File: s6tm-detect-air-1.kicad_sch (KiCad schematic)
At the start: 72 parts, among them J1 Conn_01x04, J2 TC2030, J3 Conn_01x04, J4 Conn_01x04, J5 Conn_01x04_Pin, SW1 SW_Push, SW2 SW_Push, U1 SYS1002-H2, U10 004-1-0100, U2 MiCS-5524, U3 LMC6482, U4 HT753-1, U5 SN65HVD230, U6 STM32F103C8Tx, U7 HTU21, U8 LM73100, U9 ENS16x, Y1 8M

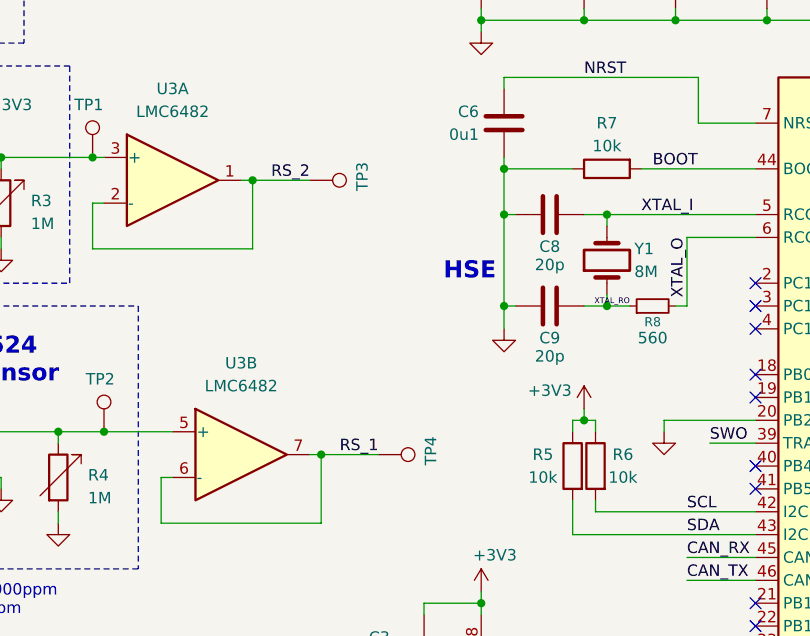
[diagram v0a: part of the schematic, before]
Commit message: pcb: import 2 layer jlc stackup
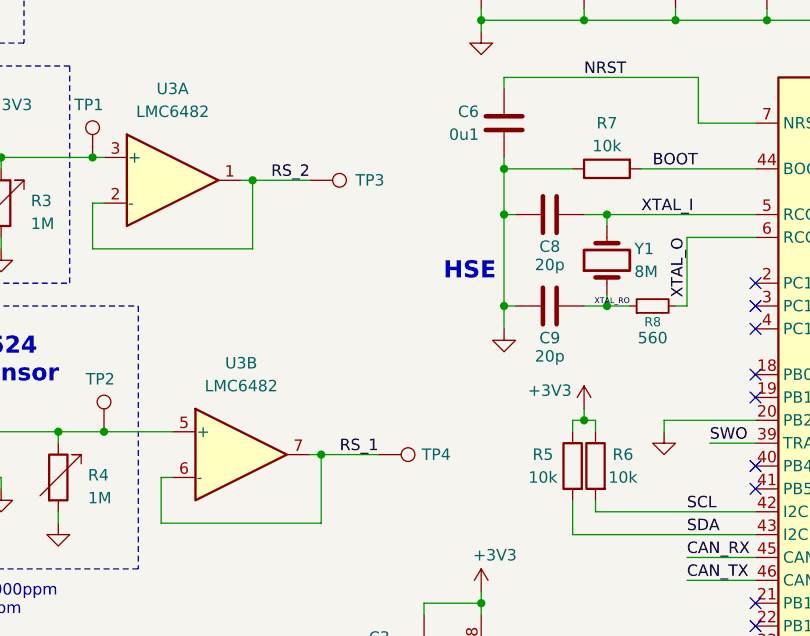
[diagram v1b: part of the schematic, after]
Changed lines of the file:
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@@
 		(dnp no)
 		(property "Reference" "TP4"
-			(at 94.742 99.568 0)
+			(at 93.726 101.6 90)
 			(show_name no)
 			(do_not_autoplace no)
@@
 		(dnp no)
 		(property "Reference" "TP3"
-			(at 87.122 69.088 0)
-			(show_name no)
-			(do_not_autoplace no)
+			(at 86.36 71.12 90)
+			(show_name no)
+			(do_not_autoplace no)

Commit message: pcb: add pwr layout
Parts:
- removed D6: H5VU10U, GLCS:Diode_DFN1006, symbol GLCS:H5VU10U
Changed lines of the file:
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@@
 	)
 	(junction
-		(at 162.56 184.15)
-		(diameter 0)
-		(color 0 0 0 0)
-	)
-	(junction
 		(at 151.13 55.88)
 		(diameter 0)
@@
 	(wire
 		(pts
-			(xy 162.56 184.15) (xy 158.75 184.15)
-		)
-		(stroke
-			(width 0)
-			(type default)
-		)
-	)
-	(wire
-		(pts
 			(xy 214.63 93.98) (xy 214.63 92.71)
 		)
@@
 	)
 	(symbol
-		(lib_id "GLCS:H5VU10U")
-		(at 158.75 187.96 90)
-		(mirror x)
-		(unit 1)
-		(body_style 1)
-		(exclude_from_sim no)
-		(in_bom yes)
-		(on_board yes)
-		(in_pos_files yes)
-		(dnp no)
-		(property "Reference" "D6"
-			(at 156.464 187.706 90)
-			(show_name no)
-			(do_not_autoplace no)
-			(effects
-				(font
-					(size 1.27 1.27)
-				)
-				(justify left)
-			)
-		)
-		(property "Value" "H5VU10U"
-			(at 156.21 189.2299 90)
-			(hide yes)
-			(show_name no)
-			(do_not_autoplace no)
-			(effects
-				(font
-					(size 1.27 1.27)
-				)
-				(justify left)
-			)
-		)
-		(property "Footprint" "GLCS:Diode_DFN1006"
-			(at 163.195 187.96 0)
-			(hide yes)
-			(show_name no)
-			(do_not_autoplace no)
-			(effects
-				(font
-					(size 1.27 1.27)
-				)
-			)
-		)
-		(property "Datasheet" "https://datasheet.lcsc.com/lcsc/2504101957_hongjiacheng-H5VU10U_C22395519.pdf"
-			(at 158.75 187.96 0)
-			(hide yes)
-			(show_name no)
-			(do_not_autoplace no)
-			(effects
-				(font
-					(size 1.27 1.27)
-				)
-			)
-		)
-		(property "Description" "-55℃~+155℃ 0.8pF 16V 200nA 55W@8/20us 5A@8/20us 5V 6V ESD IEC 61000-4-2 Unidirectional DFN1006-2L ESD and Surge Protection (TVS/ESD) ROHS"
-			(at 158.75 187.96 0)
-			(hide yes)
-			(show_name no)
-			(do_not_autoplace no)
-			(effects
-				(font
-					(size 1.27 1.27)
-				)
-			)
-		)
-		(property "Basic" "E"
-			(at 158.75 187.96 90)
-			(hide yes)
-			(show_name no)
-			(do_not_autoplace no)
-			(effects
-				(font
-					(size 1.27 1.27)
-				)
-			)
-		)
-		(property "JLCPCB Part #" "C22395519"
-			(at 158.75 187.96 90)
-			(hide yes)
-			(show_name no)
-			(do_not_autoplace no)
-			(effects
-				(font
-					(size 1.27 1.27)
-				)
-			)
-		)
-		(property "Manufacturer" "hongjiacheng"
-			(at 158.75 187.96 90)
-			(hide yes)
-			(show_name no)
-			(do_not_autoplace no)
-			(effects
-				(font
-					(size 1.27 1.27)
-				)
-			)
-		)
-		(property "Manufacturer Part Number" "H5VU10U"
-			(at 158.75 187.96 90)
-			(hide yes)
-			(show_name no)
-			(do_not_autoplace no)
-			(effects
-				(font
-					(size 1.27 1.27)
-				)
-			)
-		)
-		(pin "1"
-		)
-		(pin "2"
-		)
-		(instances
-			(project "s6tm-detect-air-1"
-				(path "/8d20b800-c106-4814-ab1a-7da2e31fcc85"
-					(reference "D6")
-					(unit 1)
-				)
-			)
-		)
-	)
-	(symbol
 		(lib_id "Connector_Generic:Conn_01x04")
 		(at 77.47 151.13 0)
@@
 					(unit 1)
 				)
-			)
-		)
-	)
-	(symbol
-		(lib_id "power:GND")
-		(at 158.75 191.77 0)
-		(mirror y)
-		(unit 1)
-		(body_style 1)
-		(exclude_from_sim no)
-		(in_bom yes)
-		(on_board yes)
-		(in_pos_files yes)
-		(dnp no)
-		(property "Reference" "#PWR037"
-			(at 158.75 198.12 0)
-			(hide yes)
-			(show_name no)
-			(do_not_autoplace no)
-			(effects
-				(font
-					(size 1.27 1.27)
-				)
-			)
-		)
-		(property "Value" "GND"
-			(at 154.686 193.548 0)
-			(hide yes)
-			(show_name no)
-			(do_not_autoplace no)
-			(effects
-				(font
-					(size 1.27 1.27)
-				)
-			)
-		)
-		(property "Footprint" ""
-			(at 158.75 191.77 0)
-			(hide yes)
-			(show_name no)
-			(do_not_autoplace no)
-			(effects
-				(font
-					(size 1.27 1.27)
-				)
-			)
-		)
-		(property "Datasheet" ""
-			(at 158.75 191.77 0)
-			(hide yes)
-			(show_name no)
-			(do_not_autoplace no)
-			(effects
-				(font
-					(size 1.27 1.27)
-				)
-			)
-		)
-		(property "Description" "Power symbol creates a global label with name \"GND\" , ground"
-			(at 158.75 191.77 0)
-			(hide yes)
-			(show_name no)
-			(do_not_autoplace no)
-			(effects
-				(font
-					(size 1.27 1.27)
-				)
-			)
-		)
-		(pin "1"
-		)
-		(instances
-			(project "s6tm-detect-air-1"
-				(path "/8d20b800-c106-4814-ab1a-7da2e31fcc85"
-					(reference "#PWR037")
-					(unit 1)
-				)

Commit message: pcb: add module layout
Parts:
- J1, J3: footprint Connector_PinHeader_2.54mm:PinHeader_1x04_P2.54mm_Horizontal -> Connector_PinHeader_2.54mm:PinHeader_1x04_P2.54mm_Vertical
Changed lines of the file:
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@@
 			)
 		)
-		(property "Footprint" "Connector_PinHeader_2.54mm:PinHeader_1x04_P2.54mm_Horizontal"
+		(property "Footprint" "Connector_PinHeader_2.54mm:PinHeader_1x04_P2.54mm_Vertical"
 			(at 77.47 151.13 0)
 			(hide yes)
@@
 			)
 		)
-		(property "Footprint" "Connector_PinHeader_2.54mm:PinHeader_1x04_P2.54mm_Horizontal"
+		(property "Footprint" "Connector_PinHeader_2.54mm:PinHeader_1x04_P2.54mm_Vertical"
 			(at 22.86 40.64 0)
 			(hide yes)

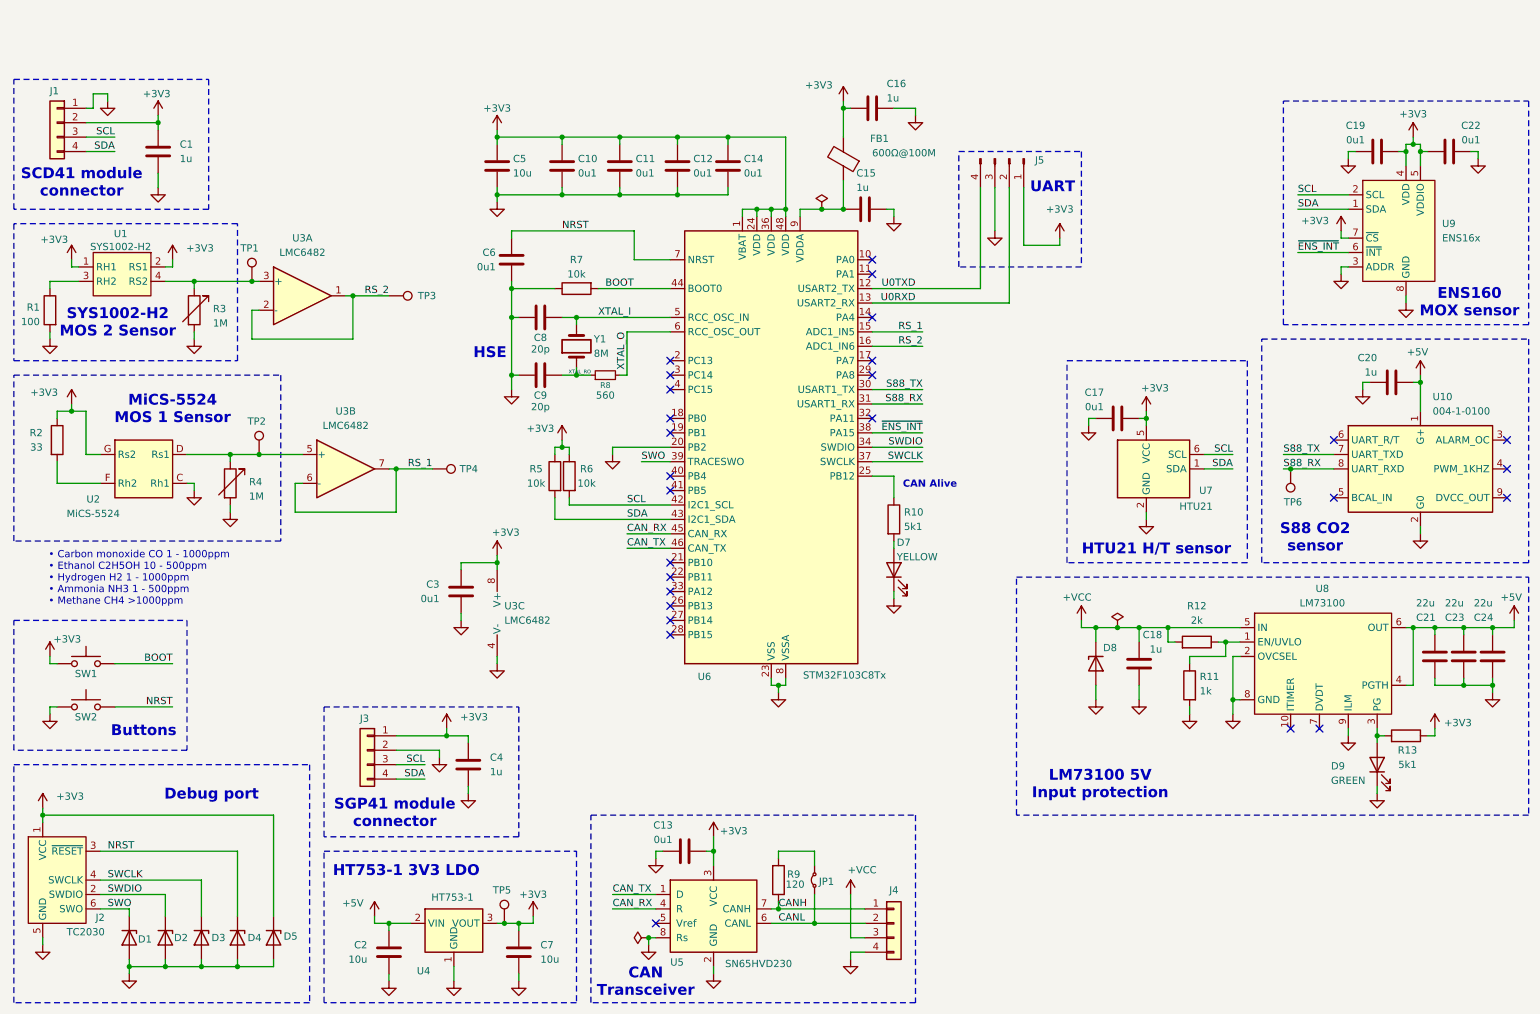
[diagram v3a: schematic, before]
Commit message: schem: add mounting & tooling holes
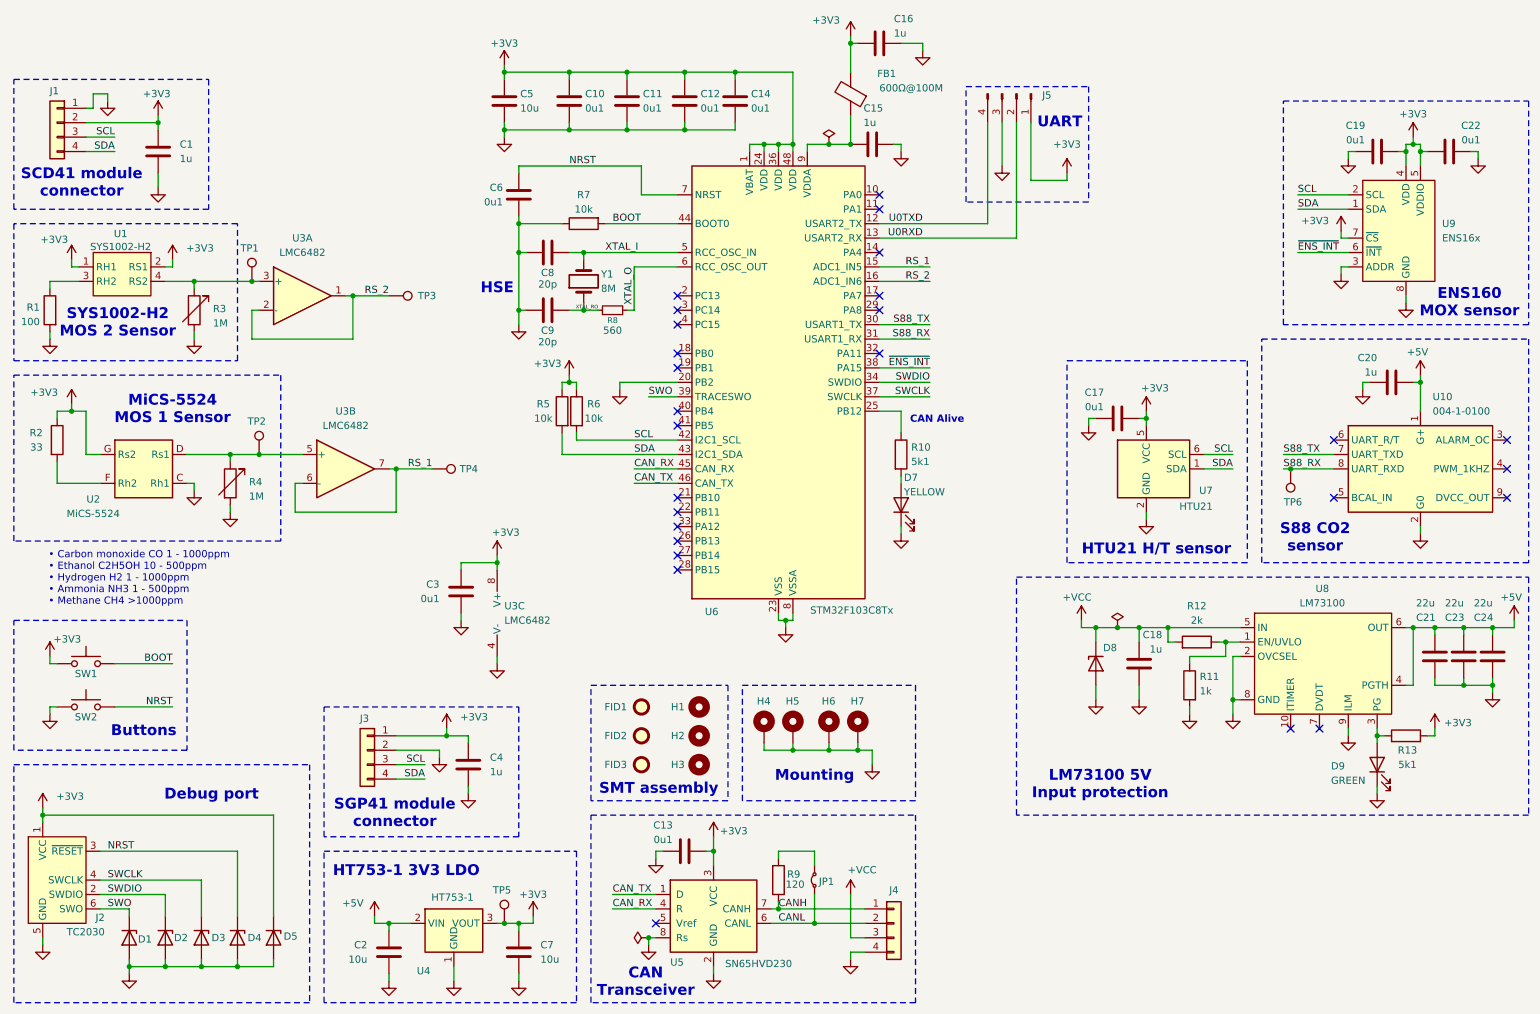
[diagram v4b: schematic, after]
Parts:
- added FID1, FID2, FID3: Fiducial, Fiducial:Fiducial_1mm_Mask2mm, symbol Mechanical:Fiducial
- added H1, H2, H3: MountingHole, MountingHole:ToolingHole_1.152mm, symbol Mechanical:MountingHole
- added H4, H5, H6, H7: MountingHole_Pad, MountingHole:MountingHole_3.2mm_M3_Pad_Via, symbol Mechanical:MountingHole_Pad
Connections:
- net GND: now also H4.1, H5.1, H6.1, H7.1
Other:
- note added: "Mounting"
- note added: "SMT assembly"
- moved on the sheet: C10, C11, C12, C14, C15, C16, C5, C6, C8, C9, D7, FB1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

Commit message: pcb/schem: add spare gpios header
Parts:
- added J6: Conn_01x08, Connector_PinHeader_2.54mm:PinHeader_2x04_P2.54mm_Horizontal, symbol Connector_Generic:Conn_01x08
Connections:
- net +3V3: now also J6.1 (Pin_1)
- net +5V: now also J6.2 (Pin_2)
- net GND: now also J6.7 (Pin_7), J6.8 (Pin_8)
- net PB13: now reaches U6.26 (PB13)
- net PB13: now also J6.4 (Pin_4)
- net PB14: now reaches U6.27 (PB14)
- net PB14: now also J6.5 (Pin_5)
- net PB15: now reaches U6.28 (PB15)
- net PB15: now also J6.6 (Pin_6)
- net PA8: now reaches U6.29 (PA8)
- net PA8: now also J6.3 (Pin_3)
- no-connect marks 27 -> 23

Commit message: pcb: add gpios routing
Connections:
- net PB13: now also U6.25 (PB12); no longer U6.26 (PB13)
- net at R10.1: now also U6.26 (PB13); no longer U6.25 (PB12)

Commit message: pcb: fix s88 rx/tx orientation
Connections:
- net S88_RX: now also U6.30 (PA9); no longer U6.31 (PA10)
- net S88_TX: now also U6.31 (PA10); no longer U6.30 (PA9)
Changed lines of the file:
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@@
 	(wire
 		(pts
+			(xy 176.53 76.2) (xy 167.64 76.2)
+		)
+		(stroke
+			(width 0)
+			(type default)
+		)
+	)
+	(wire
+		(pts
 			(xy 104.14 58.42) (xy 104.14 63.5)
 		)
@@
 	(wire
 		(pts
-			(xy 176.53 78.74) (xy 167.64 78.74)
-		)
-		(stroke
-			(width 0)
-			(type default)
-		)
-	)
-	(wire
-		(pts
 			(xy 60.96 189.23) (xy 60.96 187.96)
 		)
@@
 	(wire
 		(pts
+			(xy 176.53 78.74) (xy 167.64 78.74)
+		)
+		(stroke
+			(width 0)
+			(type default)
+		)
+	)
+	(wire
+		(pts
 			(xy 259.08 45.72) (xy 260.35 45.72)
 		)
@@
 	(wire
 		(pts
-			(xy 176.53 76.2) (xy 167.64 76.2)
-		)
-		(stroke
-			(width 0)
-			(type default)
-		)
-	)
-	(wire
-		(pts
 			(xy 219.71 132.08) (xy 218.44 132.08)
 		)
@@
 		)
 	)
+	(label "S88_RX"
+		(at 176.53 76.2 180)
+		(effects
+			(font
+				(size 1.27 1.27)
+			)
+			(justify right bottom)
+		)
+	)
 	(label "NRST"
 		(at 113.03 48.26 0)
@@
 		)
 	)
-	(label "S88_TX"
-		(at 176.53 76.2 180)
-		(effects
-			(font
-				(size 1.27 1.27)
-			)
-			(justify right bottom)
-		)
-	)
 	(label "SWDIO"
 		(at 176.53 86.36 180)
@@
 		)
 	)
+	(label "S88_TX"
+		(at 176.53 78.74 180)
+		(effects
+			(font
+				(size 1.27 1.27)
+			)
+			(justify right bottom)
+		)
+	)
 	(label "CAN_RX"
 		(at 124.46 101.6 0)
@@
 		(effects
 			(font
-				(size 1.27 1.27)
-			)
-			(justify right bottom)
-		)
-	)
-	(label "S88_RX"
-		(at 176.53 78.74 180)
-		(effects
-			(font
